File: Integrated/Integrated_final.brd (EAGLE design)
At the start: 201.9 x 77.1 mm, 73 parts, among them IC1 74AHC1G32DBV, IC2 74AHC1G08DBV, IC3 74AHC1G08DBV, IC7 74AHC1G32DBV, Q1 PSMN013-30MLC, Q2 PSMN013-30MLC, Q3 PSMN013-30MLC, Q4 PSMN013-30MLC, Q5 PSMN013-30MLC, Q6 PSMN013-30MLC, X1 5566-4, X2 5566-4

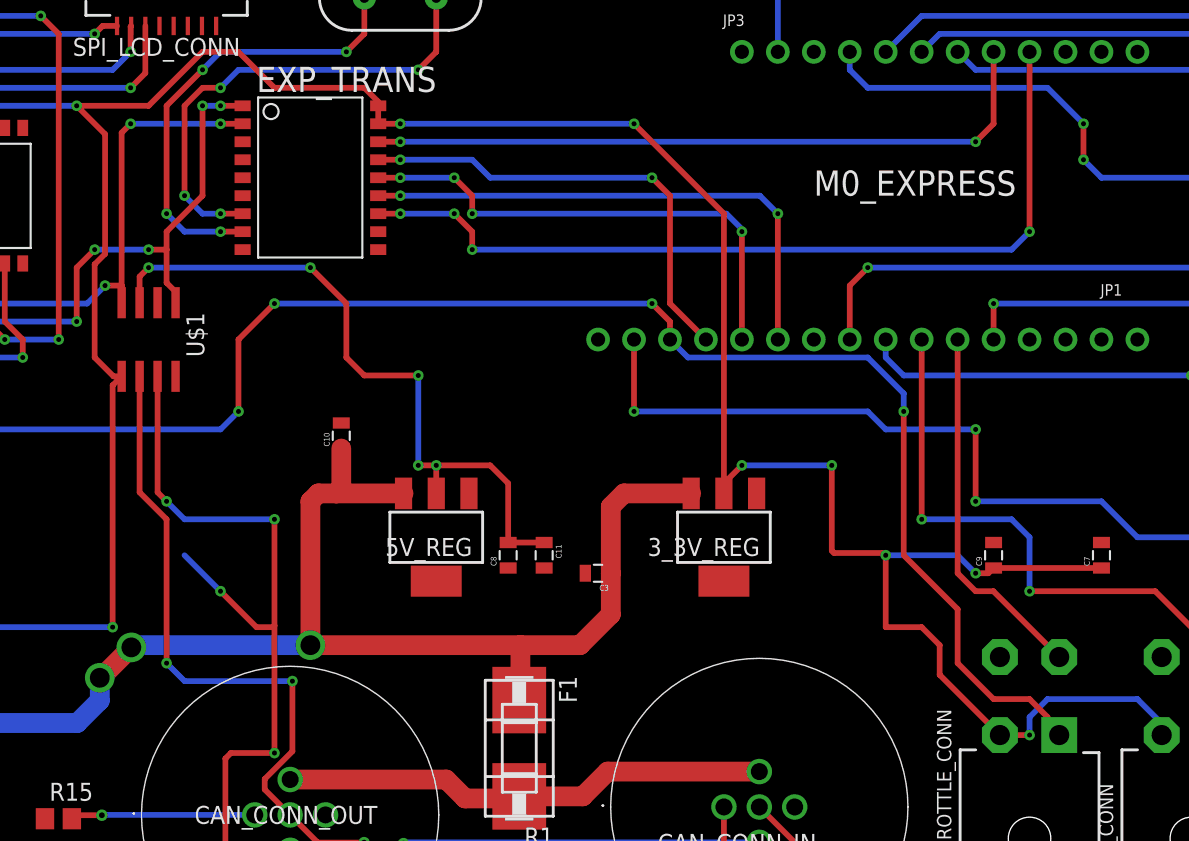
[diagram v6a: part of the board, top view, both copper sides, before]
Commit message: ripped up hanging trace
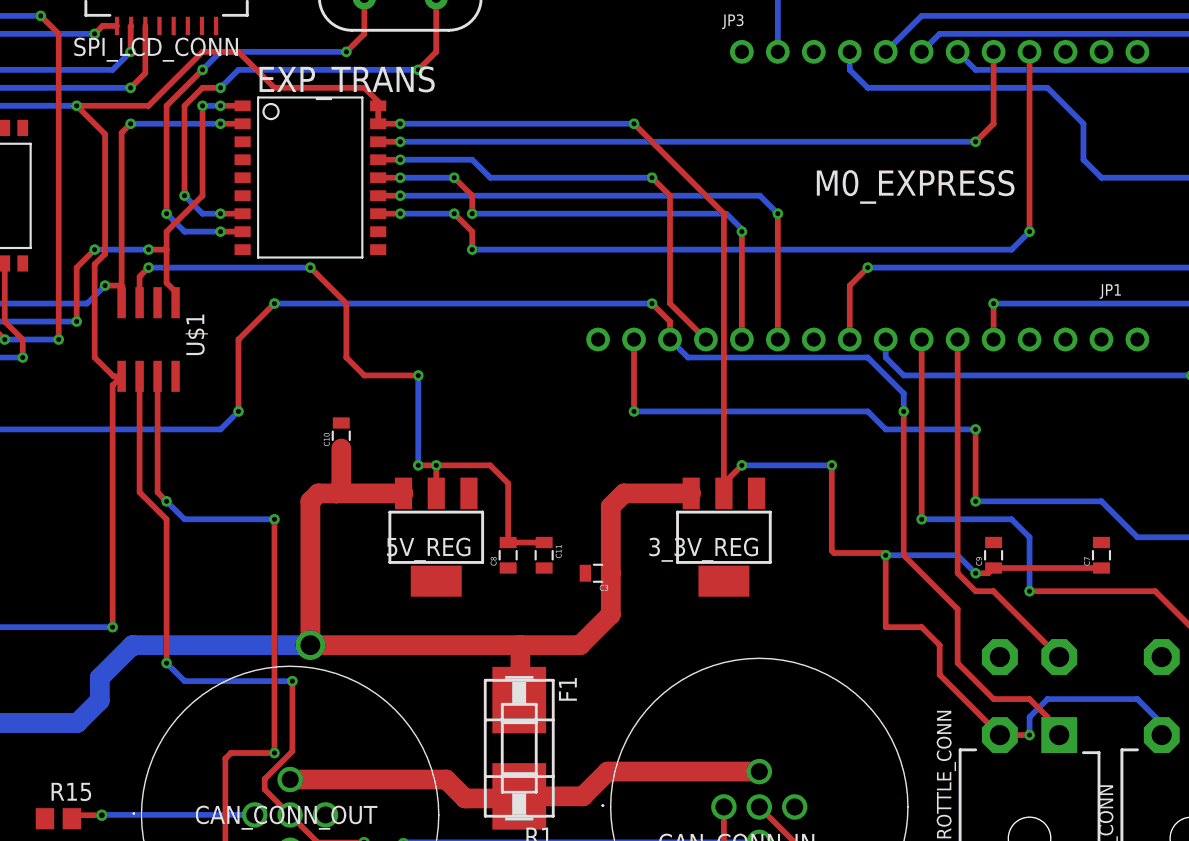
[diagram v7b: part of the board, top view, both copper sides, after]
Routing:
- net CAN_H: track 96.2 -> 87.7 mm, vias 7 -> 6
- net 12V: track 265.6 -> 265.8 mm, vias 3 -> 1
- net D13: vias 3 -> 1
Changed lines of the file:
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@@
 <wire x1="67.31" y1="36.83" x2="68.58" y2="35.56" width="0.4064" layer="16"/>
 <wire x1="68.58" y1="35.56" x2="74.93" y2="35.56" width="0.4064" layer="16"/>
-<wire x1="74.93" y1="19.05" x2="74.93" y2="28.04878125" width="0.4064" layer="1"/>
-<wire x1="74.93" y1="28.04878125" x2="74.93" y2="35.56" width="0.4064" layer="1"/>
+<wire x1="74.93" y1="19.05" x2="74.93" y2="35.56" width="0.4064" layer="1"/>
 <wire x1="66.675" y1="37.465" x2="66.675" y2="45.66" width="0.4064" layer="1"/>
 <contactref element="CAN_CONN_IN" pad="4"/>
 <contactref element="CAN_CONN_OUT" pad="4"/>
-<wire x1="68.58" y1="33.02" x2="71.12" y2="30.48" width="0.4064" layer="16"/>
-<via x="71.12" y="30.48" extent="1-16" drill="0.35"/>
-<wire x1="71.12" y1="30.48" x2="73.66" y2="27.94" width="0.4064" layer="1"/>
 <wire x1="76.03890625" y1="12.1781125" x2="71.483575" y2="12.1781125" width="0.4064" layer="16"/>
 <wire x1="71.483575" y1="12.1781125" x2="71.4644625" y2="12.159" width="0.4064" layer="16"/>
@@
 <wire x1="71.855634375" y1="19.05110625" x2="74.92889375" y2="19.05110625" width="0.4064" layer="1"/>
 <wire x1="74.92889375" y1="19.05110625" x2="74.93" y2="19.05" width="0.4064" layer="1"/>
-<wire x1="73.66" y1="27.94" x2="74.82121875" y2="27.94" width="0.4064" layer="1"/>
-<wire x1="74.82121875" y1="27.94" x2="74.93" y2="28.04878125" width="0.4064" layer="1"/>
 <wire x1="109.18" y1="12.74" x2="84.130528125" y2="12.74" width="0.4064" layer="16"/>
 <wire x1="84.130528125" y1="12.74" x2="84.0417125" y2="12.651184375" width="0.4064" layer="16"/>
@@
 <via x="151.13" y="59.69" extent="1-16" drill="0.35"/>
 <wire x1="151.13" y1="59.69" x2="133.35" y2="59.69" width="0.4064" layer="16"/>
-<wire x1="133.35" y1="59.69" x2="132.08" y2="60.96" width="0.4064" layer="16"/>
-<via x="132.08" y="60.96" extent="1-16" drill="0.35"/>
-<wire x1="132.08" y1="60.96" x2="132.08" y2="63.5" width="0.4064" layer="1"/>
-<via x="132.08" y="63.5" extent="1-16" drill="0.35"/>
+<wire x1="132.08" y1="60.96" x2="133.35" y2="59.69" width="0.4064" layer="16"/>
 <wire x1="129.54" y1="66.04" x2="116.84" y2="66.04" width="0.4064" layer="16"/>
 <wire x1="116.84" y1="66.04" x2="115.57" y2="67.31" width="0.4064" layer="16"/>
 <wire x1="115.57" y1="67.31" x2="115.57" y2="68.58" width="0.4064" layer="16"/>
-<wire x1="132.08" y1="63.5" x2="129.54" y2="66.04" width="0.4064" layer="16"/>
+<wire x1="129.54" y1="66.04" x2="132.08" y2="63.5" width="0.4064" layer="16"/>
+<wire x1="132.08" y1="63.5" x2="132.08" y2="60.96" width="0.4064" layer="16"/>
 </signal>
 <signal name="SCL">
@@
 <wire x1="77.47" y1="26.67" x2="64.97864375" y2="26.67" width="1.397" layer="16"/>
 <wire x1="64.97864375" y1="26.67" x2="64.820375" y2="26.51173125" width="1.397" layer="16"/>
-<via x="64.820375" y="26.51173125" extent="1-16" drill="1.397"/>
-<wire x1="64.820375" y1="26.51173125" x2="63.003371875" y2="24.694728125" width="1.397" layer="1"/>
-<wire x1="63.003371875" y1="24.694728125" x2="62.921178125" y2="24.694728125" width="1.397" layer="1"/>
-<wire x1="62.921178125" y1="24.694728125" x2="62.590884375" y2="24.364434375" width="1.397" layer="1"/>
-<via x="62.590884375" y="24.364434375" extent="1-16" drill="1.397"/>
 <wire x1="62.590884375" y1="24.364434375" x2="62.590884375" y2="22.75781875" width="1.397" layer="16"/>
 <wire x1="62.590884375" y1="22.75781875" x2="61.003965625" y2="21.1709" width="1.397" layer="16"/>
@@
 <wire x1="79.650546875" y1="40.561125" x2="79.650546875" y2="37.728646875" width="1.397" layer="1"/>
 <wire x1="79.650546875" y1="37.728646875" x2="79.3109" y2="37.389" width="1.397" layer="1"/>
+<wire x1="64.97864375" y1="26.67" x2="64.89645" y2="26.67" width="1.397" layer="16"/>
+<wire x1="64.89645" y1="26.67" x2="62.590884375" y2="24.364434375" width="1.397" layer="16"/>
 <wire x1="92.222365625" y1="22.7886875" x2="92.222365625" y2="15.9886875" width="0" layer="19" extent="1-1"/>
 </signal>
